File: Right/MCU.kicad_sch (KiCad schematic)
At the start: 35 parts, among them U29 Button, U30 nRF52840_aQFN73, X1 32.768 kHz, X2 32MHZ

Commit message: worked on right hand
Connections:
- net P0.05 renamed P1.05
- no-connect marks 2 -> 3

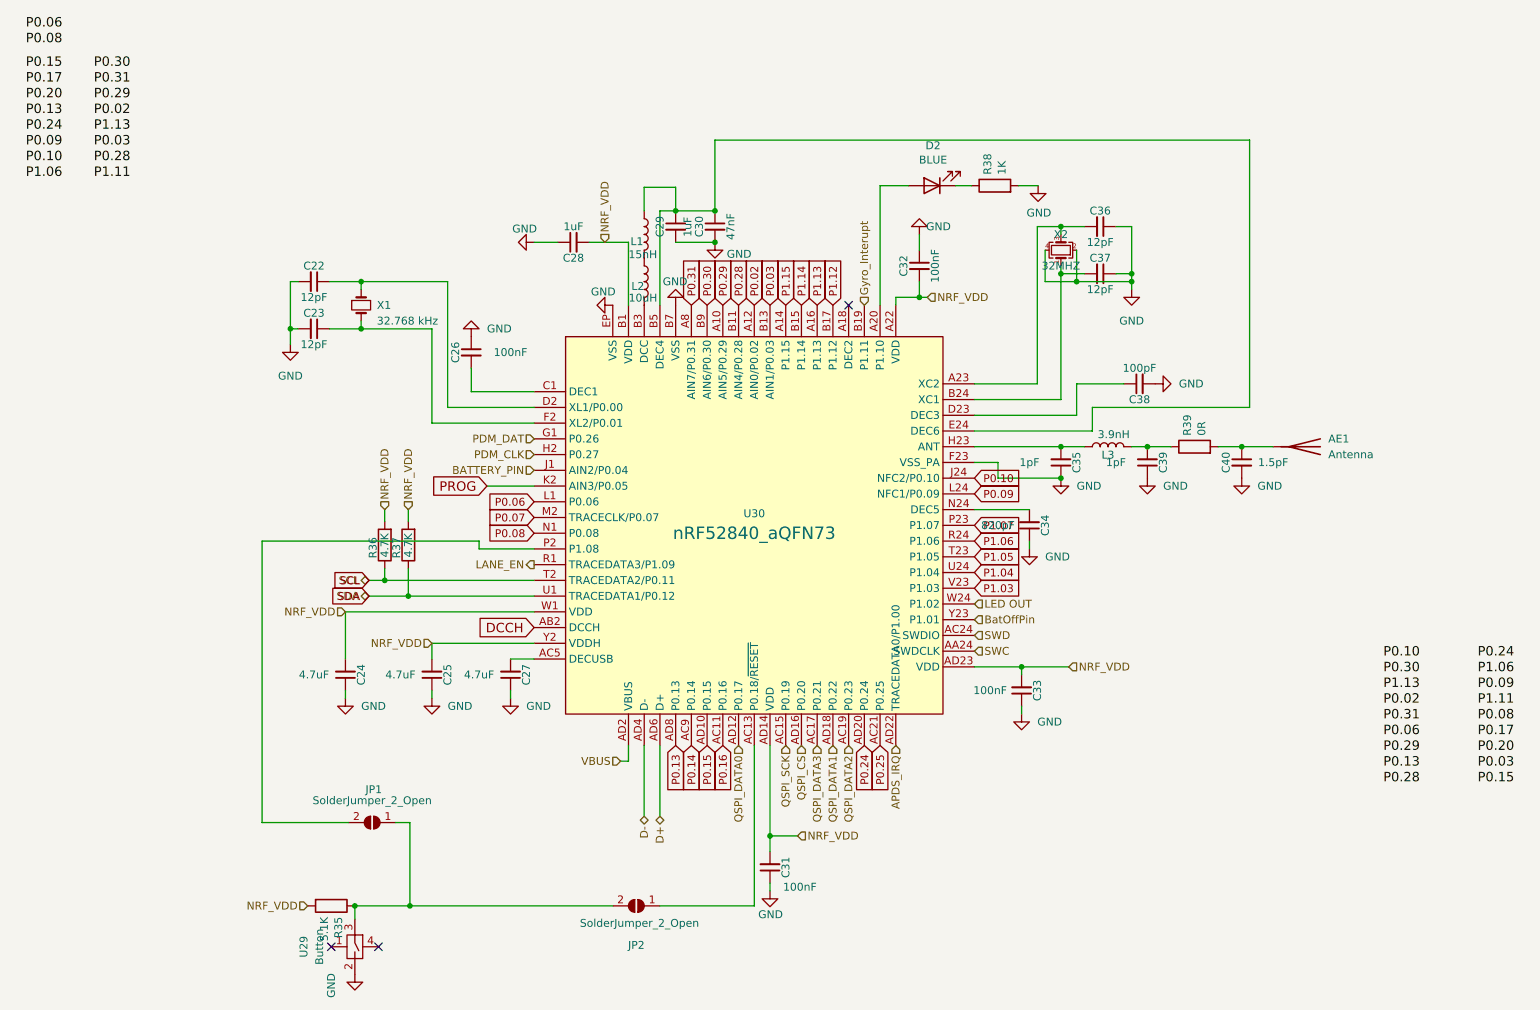
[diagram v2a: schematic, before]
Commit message: upgraded files to kicad7
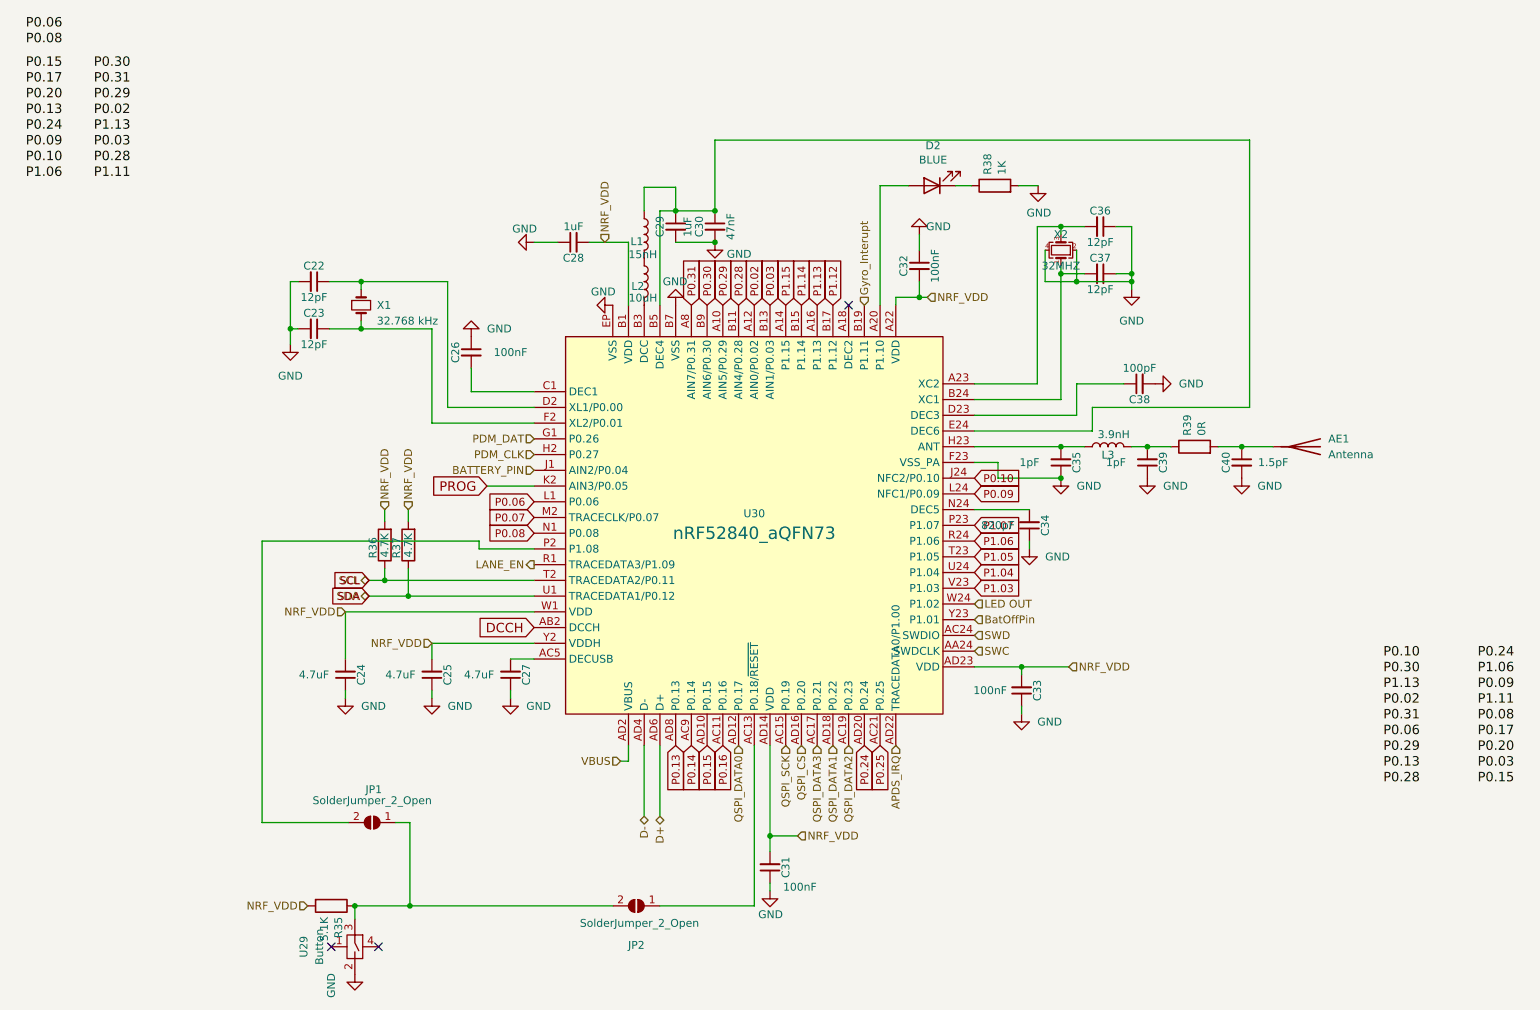
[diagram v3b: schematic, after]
